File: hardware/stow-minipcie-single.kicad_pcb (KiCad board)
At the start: 2 copper layers, 30 x 51 mm, 10 parts, among them P1 mPCIe, P2 USB, U1 SM200, U2 FT232RL

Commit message: Route the whole board.
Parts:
- U2: footprint Housings_SSOP:SSOP-24_5.3x8.2mm_Pitch0.65mm -> Housings_SSOP:SSOP-28_5.3x10.2mm_Pitch0.65mm
- turned XTAL1 to 270 degrees
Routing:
- net GND: track 0.00 -> 161.2 mm, vias 0 -> 20
- net FT_3v3: track 0.00 -> 87.8 mm, vias 0 -> 6
- net VCC: track 0.00 -> 78.6 mm, vias 0 -> 3
- net USB_D-: track 0.00 -> 77.8 mm, vias 0 -> 4
- net USB_D+: track 0.00 -> 75.7 mm, vias 0 -> 3
- net LED_WPAN: track 0.00 -> 50.8 mm, vias 0 -> 1
- net LED_WLAN: track 0.00 -> 47.9 mm, vias 0 -> 1
- net LED_WWAN: track 0.00 -> 39.3 mm, vias 0 -> 1
- net FT_RI: track 0.00 -> 35.7 mm, vias 0 -> 2
- net SLEEP: track 0.00 -> 34.7 mm
- net FT_RTS: track 0.00 -> 32.2 mm, vias 0 -> 2
- net RESET: track 0.00 -> 23.7 mm, vias 0 -> 2
- net PWREN: track 0.00 -> 23.3 mm, vias 0 -> 3
- net FT_RX: track 0.00 -> 21.6 mm, vias 0 -> 2
- net FT_TX: track 0.00 -> 18.9 mm, vias 0 -> 2
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- added copper zone on B.Cu, net GND
- added copper zone on F.Cu, net GND
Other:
- net class Default: trace_width 0.254 -> 0.2; via_dia 0.889 -> 0.5; via_drill 0.635 -> 0.35
- rule trace_min: 0.254 -> 0
- rule via_min_drill: 0.508 -> 0
- rule via_min_size: 0.889 -> 0

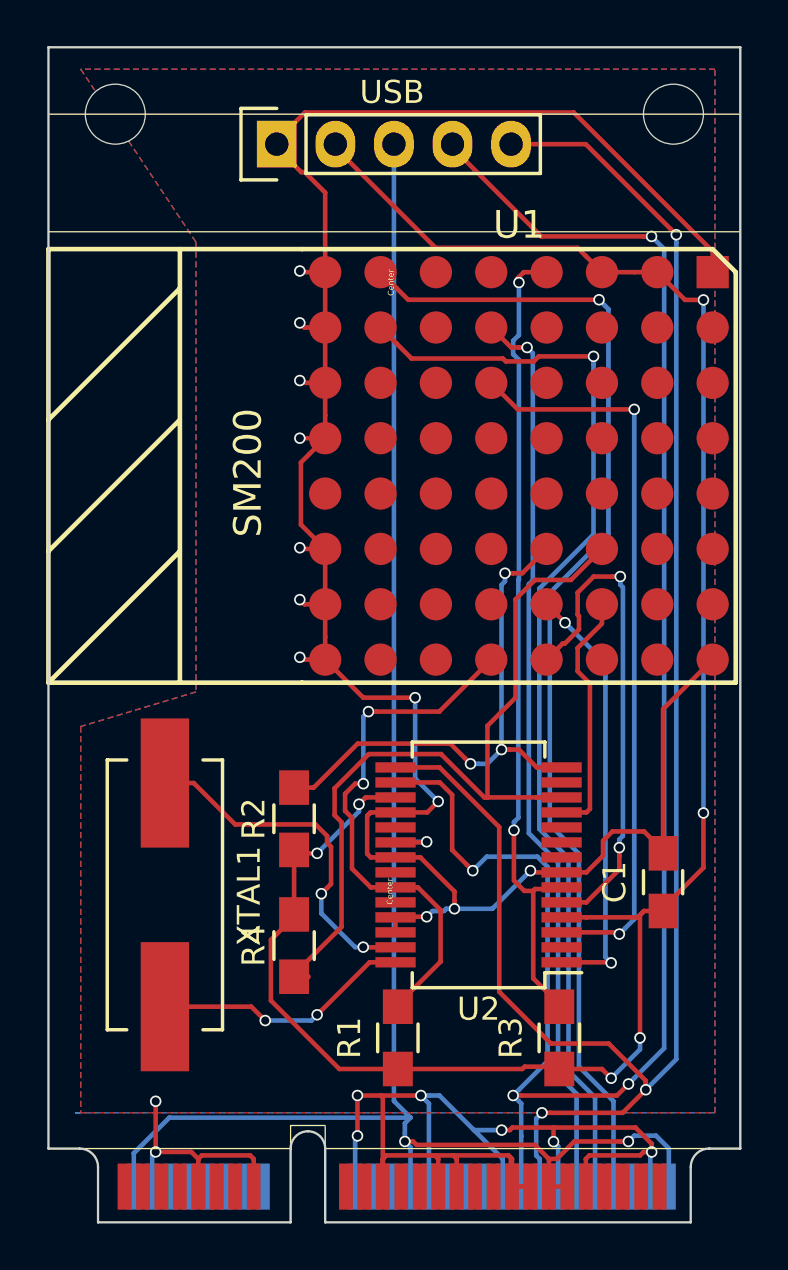
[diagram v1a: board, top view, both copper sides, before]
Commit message: Move and add silkscreen labels.
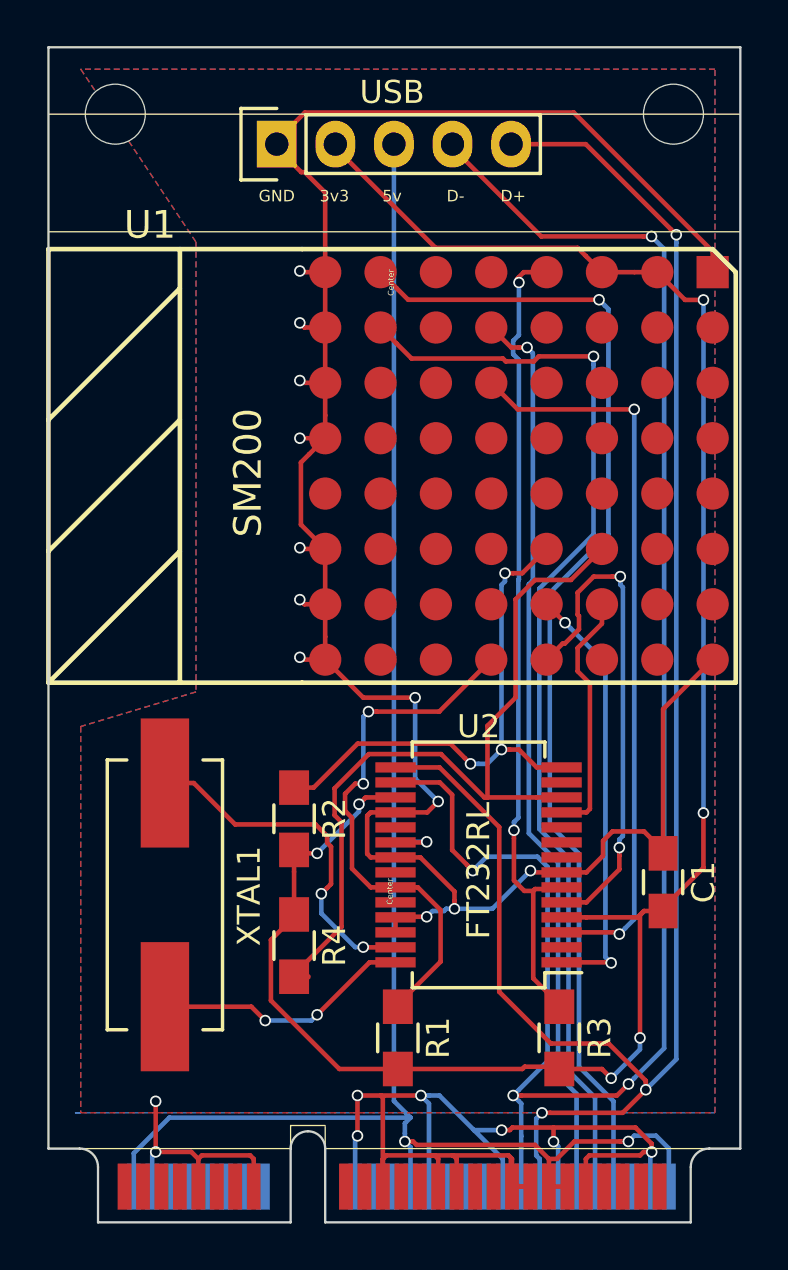
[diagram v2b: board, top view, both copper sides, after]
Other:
- board text added: "3v3"
- board text added: "5v"
- board text added: "D+"
- board text added: "D-"
- board text added: "GND"
